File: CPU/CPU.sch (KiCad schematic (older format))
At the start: 15 parts, among them J101 Conn_02x10_Odd_Even, J102 Conn_01x07_Female, Q101 IRLML0040TR, Q102 IRLML0040TR, SW101 SW_SPDT

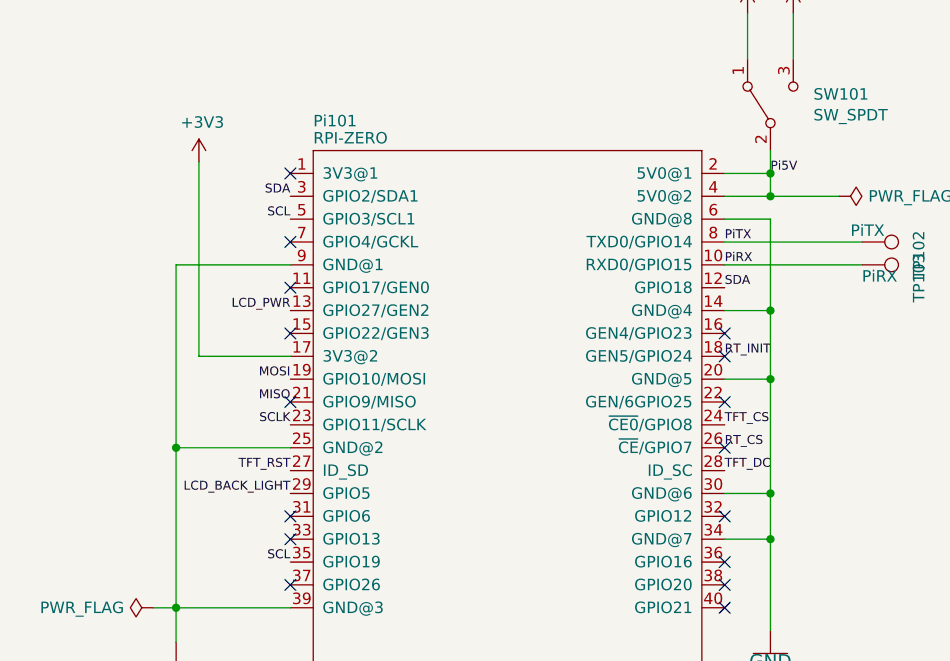
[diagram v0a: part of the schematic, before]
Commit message: Fix placement of the RPi, prepare for V5.
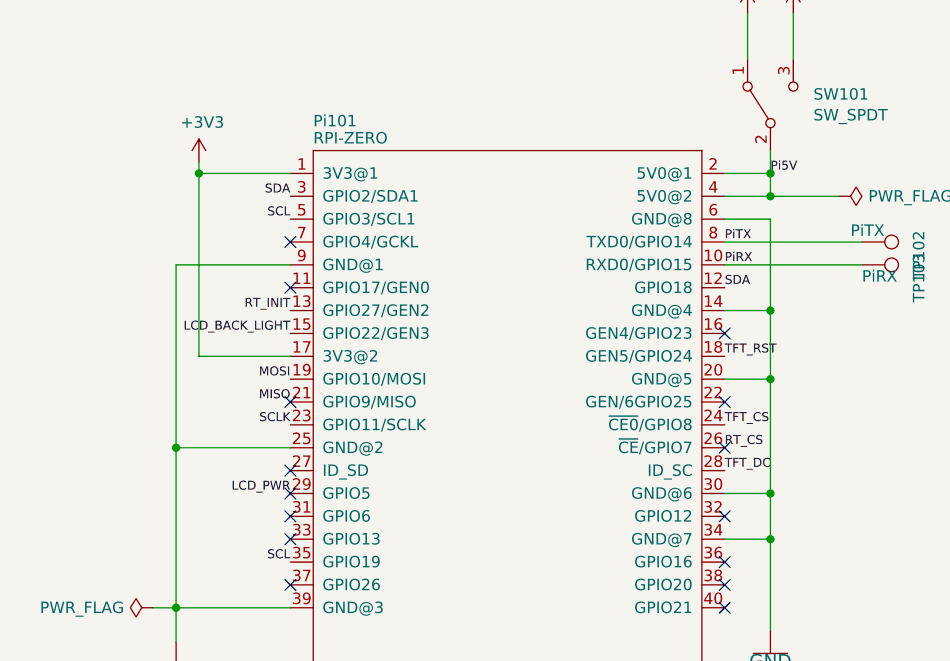
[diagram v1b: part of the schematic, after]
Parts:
- J101: DigiKey NRPN102MAMP-RC -> TMM-105-06-L-D-SM-A
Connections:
- net +3V3: now also Pi101.1 (3V3@1)
- net LCD_BACK_LIGHT: now also Pi101.15 (GPIO22/GEN3); no longer Pi101.29 (GPIO5)
- net LCD_PWR: now also Pi101.29 (GPIO5); no longer Pi101.13 (GPIO27/GEN2)
- net RT_INIT: now also Pi101.13 (GPIO27/GEN2); no longer Pi101.18 (GEN5/GPIO24)
- net TFT_RST: now also Pi101.18 (GEN5/GPIO24); no longer Pi101.27 (ID_SD)
- no-connect marks 19 -> 18
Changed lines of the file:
@@
 F 3 "~" H 1850 1700 50  0001 C CNN
 F 4 "C135211" H 1850 1700 50  0001 C CNN "LCSC Part Number"
-F 5 "NRPN102MAMP-RC" H 1850 1700 50  0001 C CNN "DigiKey"
+F 5 "TMM-105-06-L-D-SM-A" H 1850 1700 50  0001 C CNN "DigiKey"
 F 6 "CR101-V3" H 1850 1700 50  0001 C CNN "Customer Reference"
 	1    1850 1700
@@
 Text Label 4950 6100 0    39   ~ 0
 TFT_CS
-Text Label 4950 5800 0    39   ~ 0
+Text Label 3050 5600 2    39   ~ 0
 RT_INIT
 NoConn ~ 1450 1500
@@
 Text Label 4850 800  0    39   ~ 0
 PI_RESET_TOGGLE
-NoConn ~ 3050 5700
 NoConn ~ 3050 5500
 NoConn ~ 3050 5300
@@
 	1    0    0    -1
 $EndComp
-NoConn ~ 3050 5000
 Text Label 3950 2100 2    39   ~ 0
 SCL5
@@
 Text Label 5550 2800 2    39   ~ 0
 LCD_BACK_LIGHT
-Text Label 3050 6400 2    39   ~ 0
+Text Label 3050 5700 2    39   ~ 0
 LCD_BACK_LIGHT
 $Comp
@@
 Wire Wire Line
 	3300 2500 3300 2700
-Text Label 3050 5600 2    39   ~ 0
+Text Label 3050 6400 2    39   ~ 0
 LCD_PWR
 Wire Wire Line
-	2650 5800 2650 4950
+	2650 5800 2650 5000
 Wire Wire Line
 	2650 5800 3050 5800
@@
 NoConn ~ 3050 6000
 NoConn ~ 4950 6200
-NoConn ~ 4950 5800
 Text Label 6400 2150 0    39   ~ 0
 TFT_RST
-Text Label 3050 6300 2    39   ~ 0
+Text Label 4950 5800 0    39   ~ 0
 TFT_RST
 Text Label 3050 5200 2    39   ~ 0
@@
 	2900 1200 2900 1100
 Connection ~ 2600 1200
+Wire Wire Line
+	3050 5000 2650 5000
+Connection ~ 2650 5000
+Wire Wire Line
+	2650 5000 2650 4950
+NoConn ~ 3050 6400
+NoConn ~ 3050 6300
 $EndSCHEMATC
